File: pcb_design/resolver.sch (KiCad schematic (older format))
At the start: 0 parts

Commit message: Resolver routed using push pull buffer
Signed-off-by: Marcos Chaparro <mchaparro@paltatech.com>
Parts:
- added C73, C74, C75, C77, C81, C82, C83, C84, C85: 100nF, IPC7351-Nominal:CAPC1608X55, symbol C-0603
- added C76, C78: 4.7uF, IPC7351-Nominal:CAPC1608X55, symbol C-0603
- added C79, C80: 15p, IPC7351-Nominal:CAPC1608X55, symbol C
- added D21, D22, D23, D24: 1N4148W, smd-semi:SOD-123, symbol 1N4148W
- added E5: BEAD-220ohm@100khz, IPC7351-Nominal:INDC2012X130, symbol BEAD-0805
- added Q4, Q5: BC846BPDW1, smd-semi:SOT-363, symbol BC846BPDW1
- added R124, R125: 68k, IPC7351-Nominal:RESC1608X50, symbol R-0603
- added R126, R127, R128, R129, R130, R131, R132, R133: 10k, IPC7351-Nominal:RESC1608X50, symbol R-0603
- added R134, R137, R138, R141: 2.2k, IPC7351-Nominal:RESC1608X50, symbol R-0603
- added R135, R136, R139, R140: 3.3R, IPC7351-Nominal:RESC1608X50, symbol R-0603
- added R142, R143, R144, R145: 4.7R, IPC7351-Nominal:RESC2012X50, symbol R-0805
- added U15: AD2S1205, IPC7351-Nominal:QFP80P1200X1200X160-44, symbol AD2S1205
- added U18: SN74ALVC08PWR, IPC7351-Nominal:SOP65P640X110-14, symbol SN74ALVC08PWR
- added U19: OPA2376AID, IPC7351-Nominal:SOIC127P600X175-8, symbol OPA2376AID
- added X1: ABM3B - 8MHz, IPC7351-Nominal:OSCCC320X500X150, symbol XTAL-ABRACON-ABM3B
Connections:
- net labels added: +12, +3.3, +5, GND, ~RES_FAULT
- net labels removed: MOSI, ~FAULT
- wire segments 0 -> 137
- no-connect marks 0 -> 15
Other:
- note added: "5v tolerant?"
- note added: "Buffer"
- note added: "Resolver interface"
- note added: "doesn't support 12v!"
- note added: "needs voltage supervisor for ~RESET"

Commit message: Resolver routed. Added 12v regulator. The screw terminals were backwards(!). Started clearing up DRC markers.
Signed-off-by: Marcos Chaparro <mchaparro@paltatech.com>
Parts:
- removed D21, D22, D23, D24: 1N4148W, smd-semi:SOD-123, symbol 1N4148W
- removed Q4, Q5: BC846BPDW1, smd-semi:SOT-363, symbol BC846BPDW1
- removed R134, R137, R138, R141: 2.2k, IPC7351-Nominal:RESC1608X50, symbol R-0603
- removed R135, R136, R139, R140: 3.3R, IPC7351-Nominal:RESC1608X50, symbol R-0603
- removed R142, R143, R144, R145: 4.7R, IPC7351-Nominal:RESC2012X50, symbol R-0805
- removed U18: SN74ALVC08PWR, IPC7351-Nominal:SOP65P640X110-14, symbol SN74ALVC08PWR
- added C86, C87: 100nF, IPC7351-Nominal:CAPC1608X55, symbol C-0603
- added C88, C89: 22uF, IPC7351-Nominal:CAPC2012X70, symbol C-0805
- added E6: BEAD-220ohm@100khz, IPC7351-Nominal:INDC2012X130, symbol BEAD-0805
- added U18: AND3, smd-semi:SC-70-6, symbol AND3
- added U20: APX809, smd-semi:SOT-23, symbol APX809
- added U21: NCV78Mxx, smd-semi:TO-252, symbol NCV78Mxx
- C83, C84: value 100nF -> 120pF
- R127, R129: value 10k -> 22k
- R132, R133: value 10k -> 15.4k
- U19: value OPA2376AID -> AD8397; BOM IC TI OPA2376AID -> IC AD8397ARZ; mfg# OPA2376AIDR -> AD8397ARZ
- U19: value OPA2376AID -> AD8397; BOM IC TI OPA2376AID -> IC AD8397ARZ; mfg# (none) -> AD8397ARZ
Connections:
- net labels added: +24, EXC_SOURCE+, EXC_SOURCE-
- net labels removed: ~RD
- wire segments 137 -> 110
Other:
- note added: "RESET line requires\na voltage monitor"
- note added: "This is an alternative buffer suggested here:\nhttp://www.analog.com/en/analog-dialogue/articles/precision-rtdc-measures-angular-position-and-velocity.html\nIts more expensive, but much simpler and smaller"
- note removed: "5v tolerant?"
- note removed: "doesn't support 12v!"
- note removed: "needs voltage supervisor for ~RESET"
- moved on the sheet: C73, C74, C76, C77, C78, C79, C80, C81, C82, C83, C84, C85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

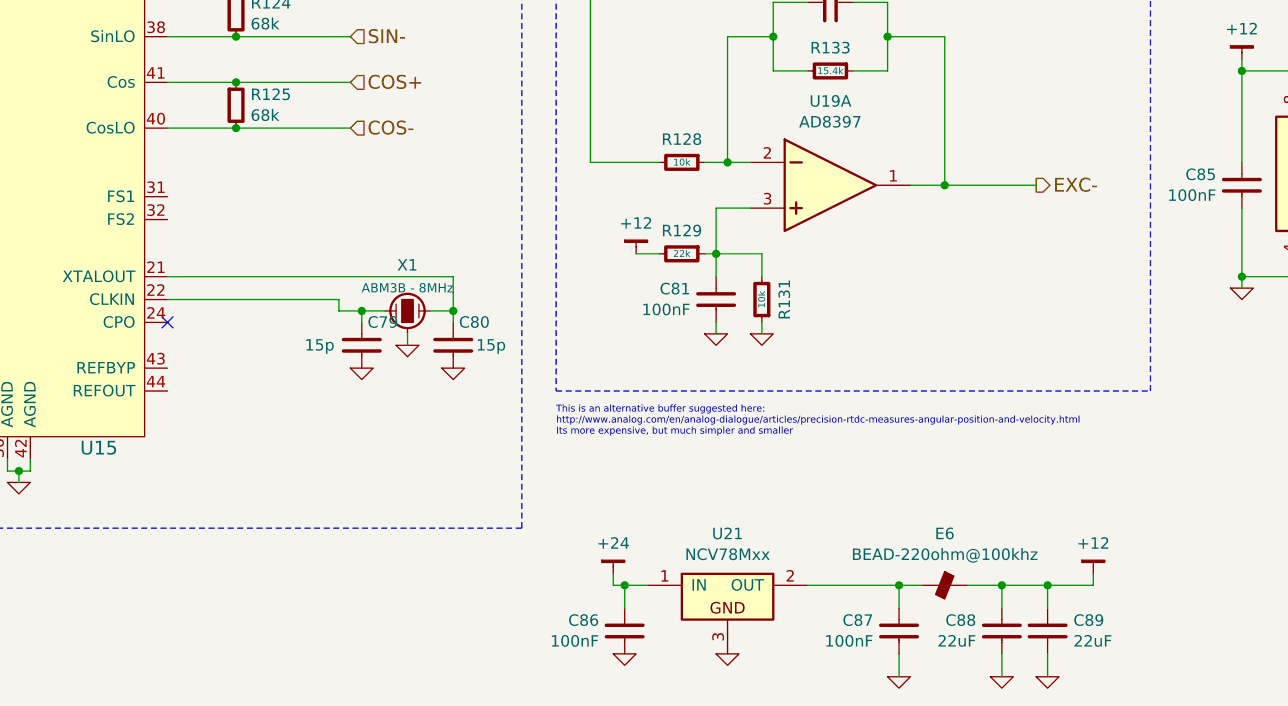
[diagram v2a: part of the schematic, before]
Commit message: Routing complete. Added 3D models. No DRC errors, a few ERC warnings
Signed-off-by: Marcos Chaparro <mchaparro@paltatech.com>
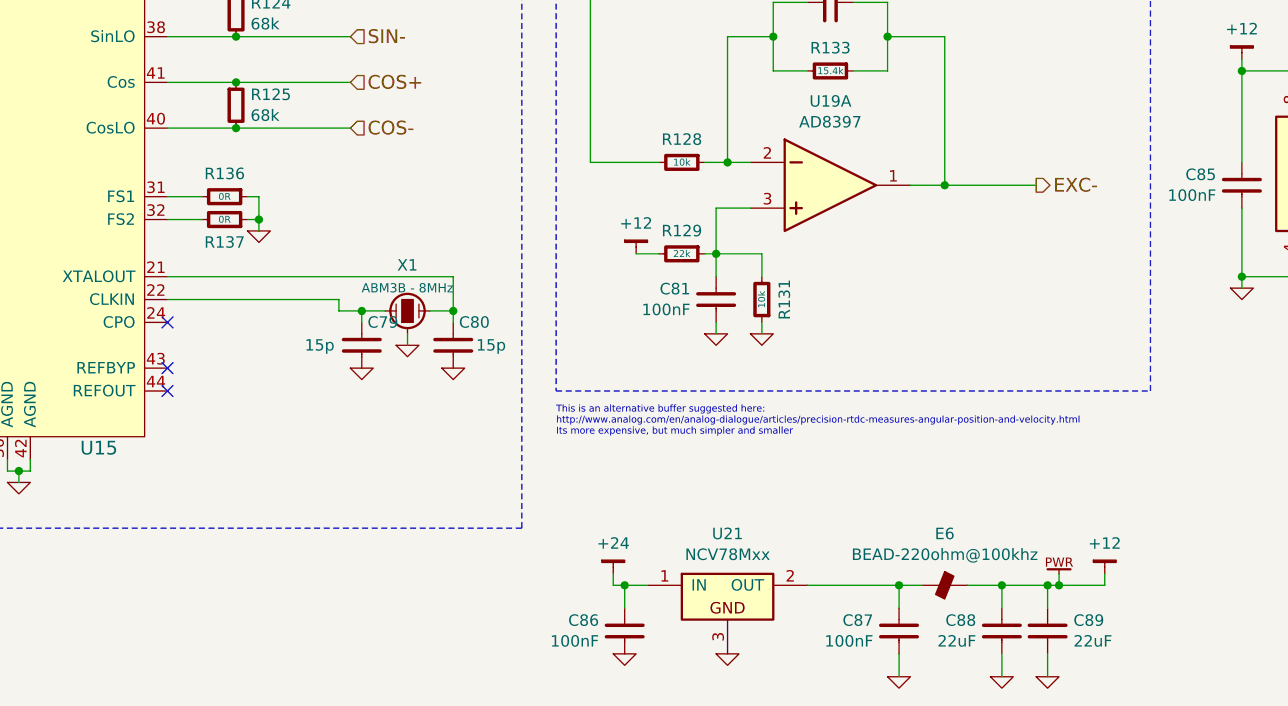
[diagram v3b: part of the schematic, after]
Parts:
- added R136, R137: 0R, IPC7351-Nominal:RESC1608X50, symbol R-0603
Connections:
- net GND: now also R136.1, R137.1
- net at U15.31 (FS1): now also R136.2
- net at U15.32 (FS2): now also R137.2
- no-connect marks 15 -> 17

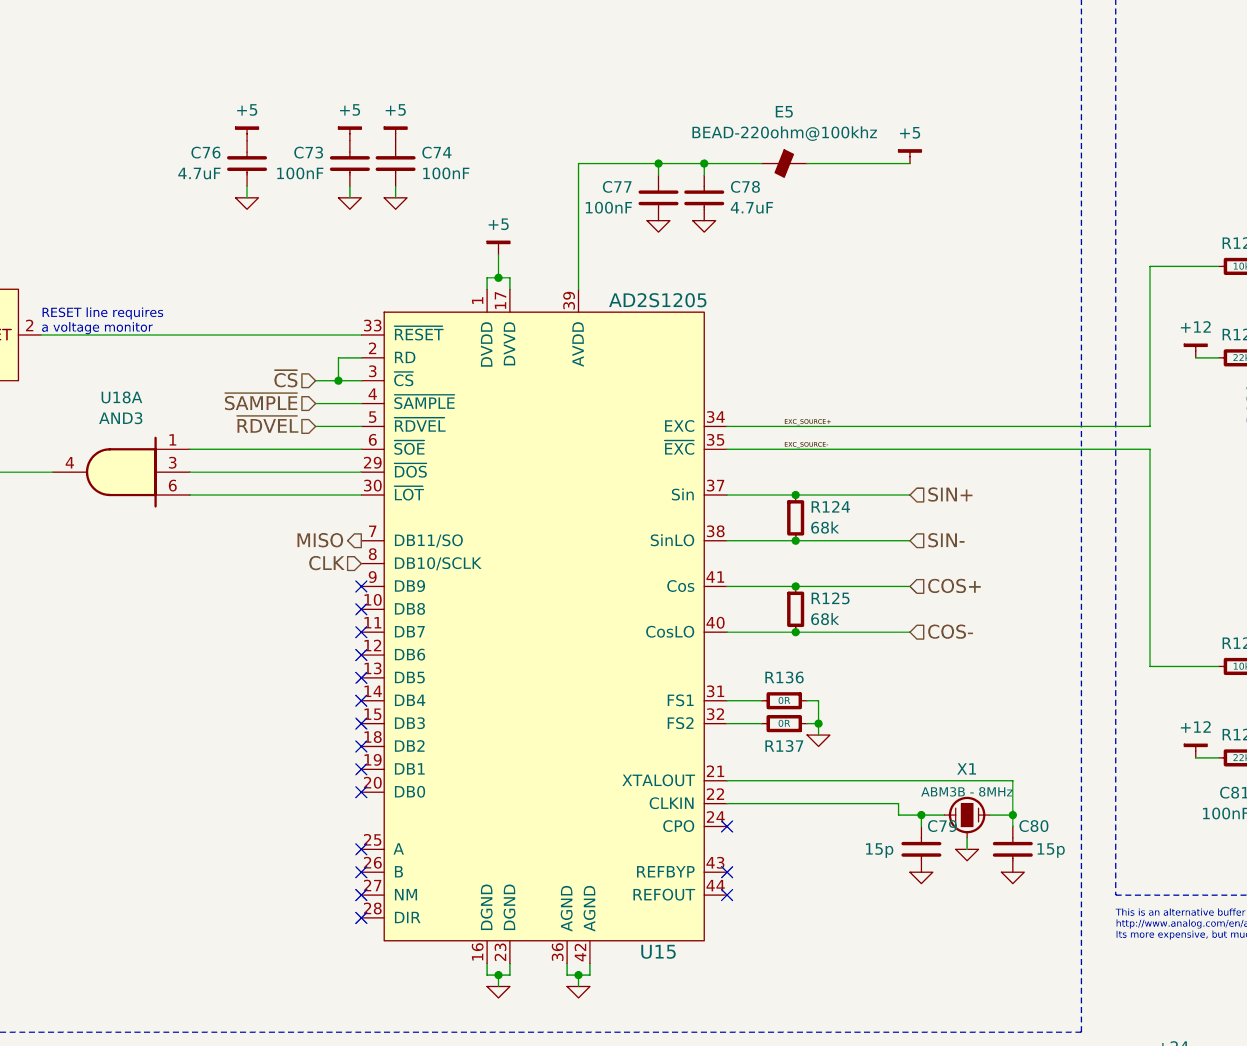
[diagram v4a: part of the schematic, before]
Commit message: Completed some part numbers
Signed-off-by: Marcos Chaparro <mchaparro@paltatech.com>
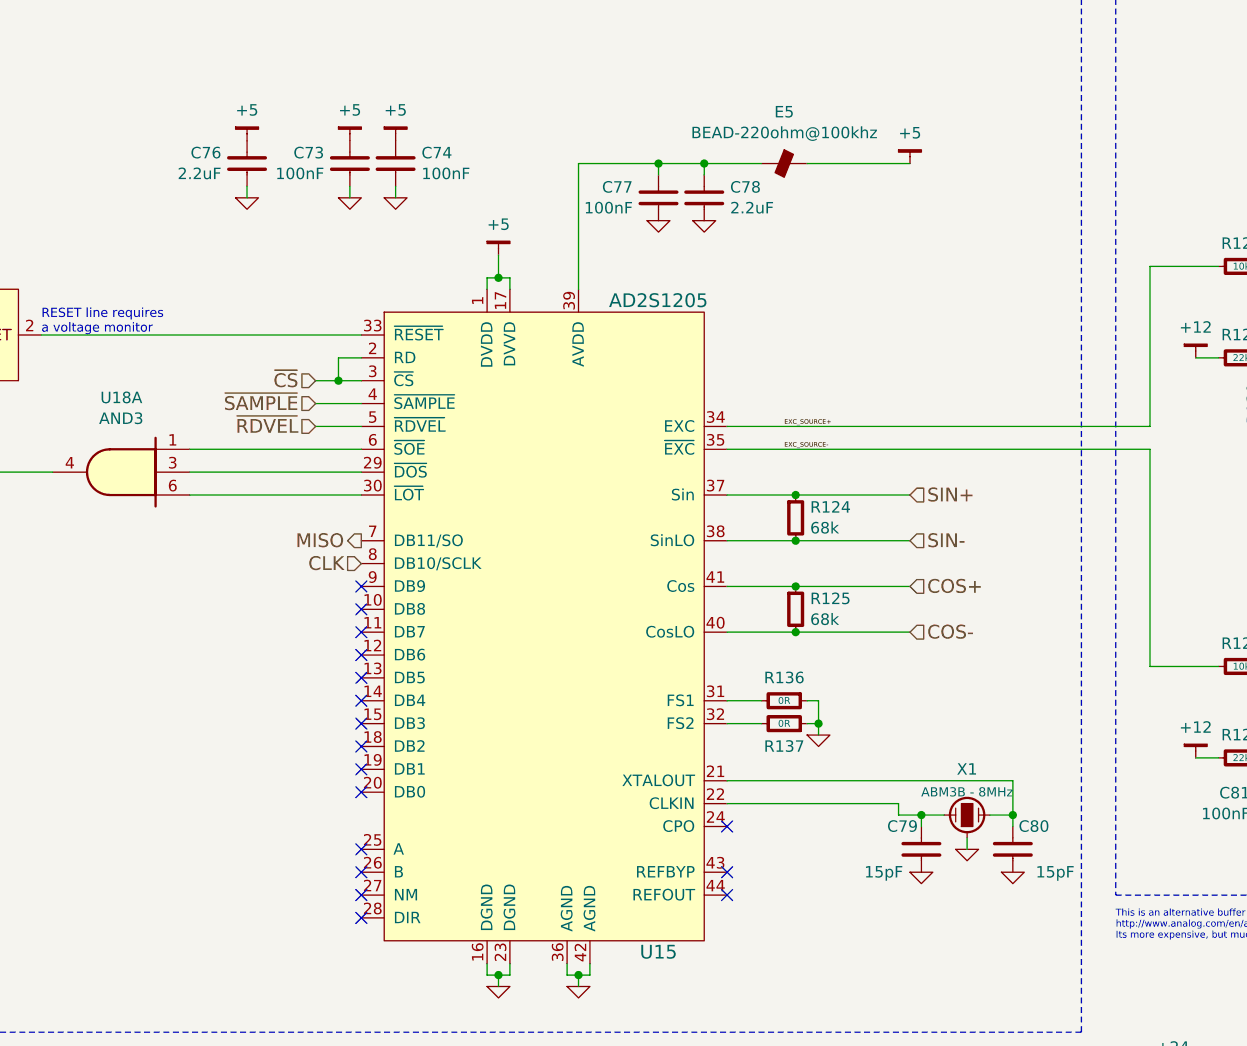
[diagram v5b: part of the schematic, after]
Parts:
- C73, C74, C75, C77, C81, C82, C85, C86, C87: MFR (none) -> Murata Electronics North America; MPN (none) -> GRM188R71E104KA01D; SPN (none) -> 490-1524-1-ND; SPR (none) -> Digikey
- C76, C78: value 4.7uF -> 2.2uF; MFR (none) -> Murata Electronics North America; MPN (none) -> GRM188R71A225KE15D; SPN (none) -> 490-4520-1-ND; SPR (none) -> Digikey
- C79, C80: value 15p -> 15pF; MFR (none) -> Murata Electronics North America; MPN (none) -> GCM1885C1H150JA16D; SPN (none) -> 490-4957-1-ND; SPR (none) -> Digikey
- C83, C84: MFR (none) -> KEMET; MPN (none) -> C0603C121F5GACTU; SPN (none) -> 399-7850-1-ND; SPR (none) -> Digikey
- C88, C89: MFR (none) -> TDK Corporation; MPN (none) -> C2012X5R1V226M125AC; SPN (none) -> 445-14428-1-ND; SPR (none) -> Digikey

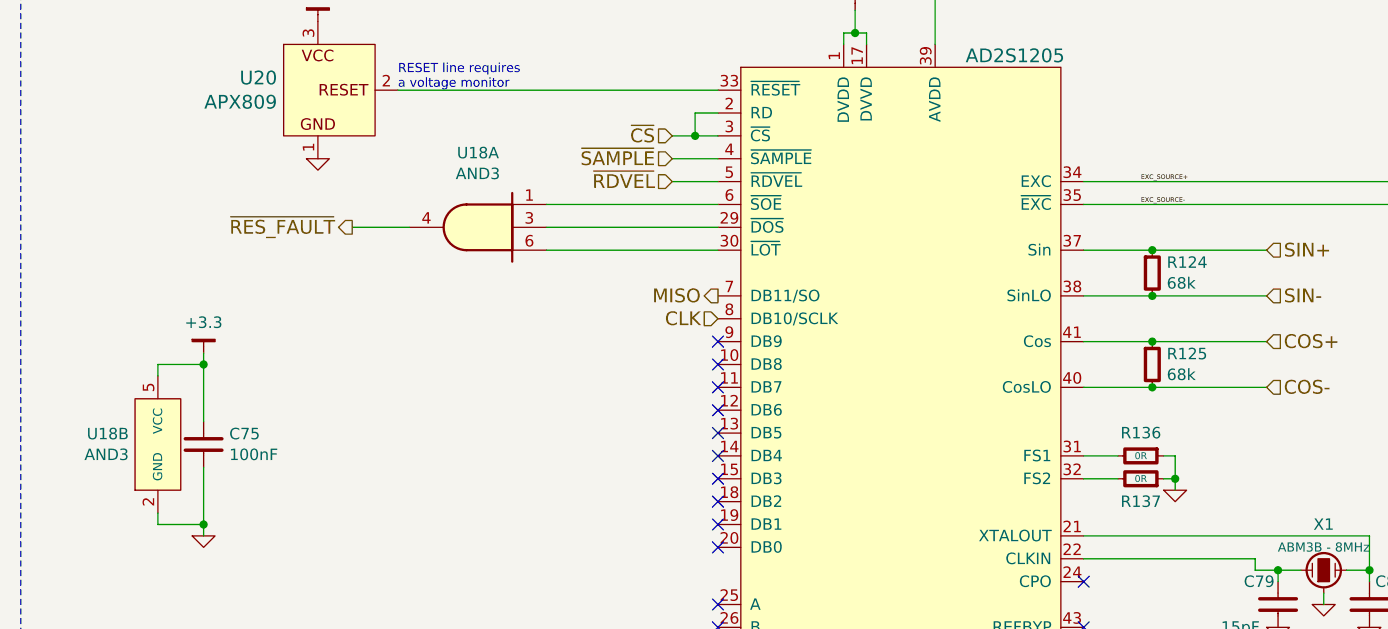
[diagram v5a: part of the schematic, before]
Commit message: Completed part number, manufacturer, etc fields. Simulated analog conditioning
Signed-off-by: Marcos Chaparro <mchaparro@paltatech.com>
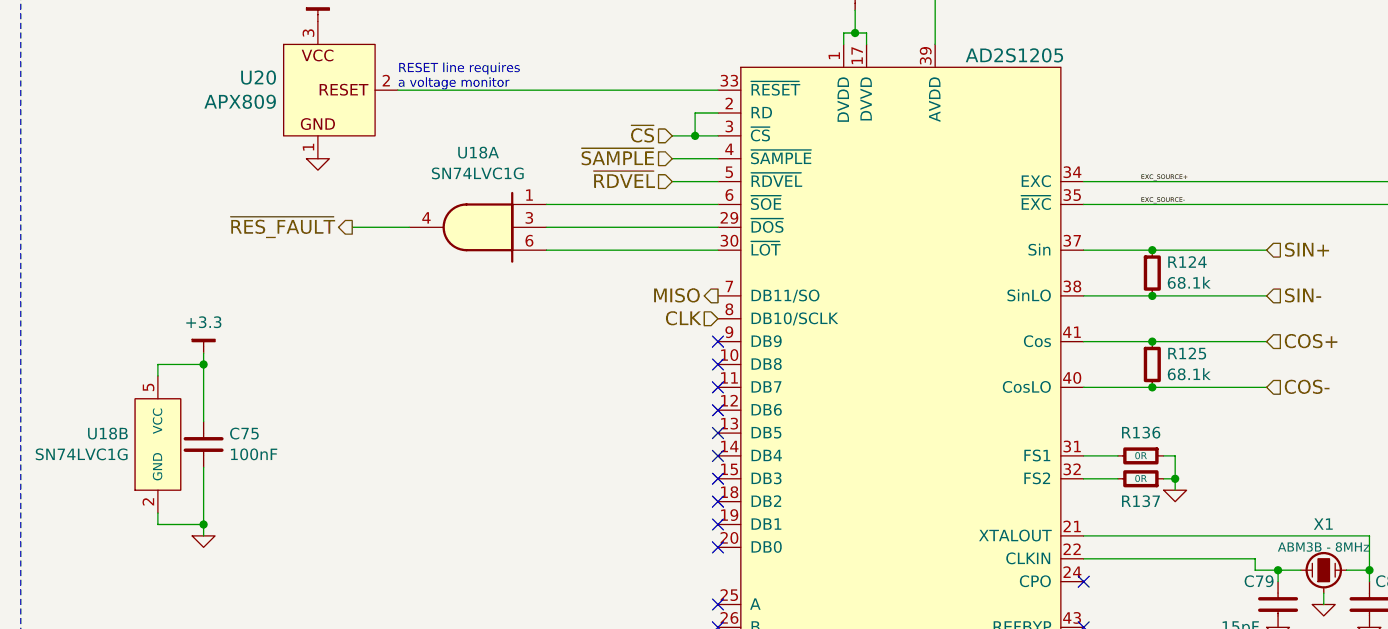
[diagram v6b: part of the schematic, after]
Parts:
- E5, E6: MFR (none) -> Murata Electronics North America; MPN (none) -> BLM21PG221SN1D; SPN (none) -> 490-1054-1-ND; SPR (none) -> Digikey
- R124, R125: value 68k -> 68.1k; MFR (none) -> Yageo; MPN (none) -> RC0603FR-0768K1L; SPN (none) -> 311-68.1KHRCT-ND; SPR (none) -> Digikey
- R126, R128, R130, R131: MFR (none) -> Yageo; MPN (none) -> RC0603FR-0710KL; SPN (none) -> 311-10.0KHRCT-ND; SPR (none) -> Digikey
- R127, R129: MFR (none) -> Yageo; MPN (none) -> RC0603FR-0722KL; SPN (none) -> 311-22.0KHRCT-ND; SPR (none) -> Digikey
- R132, R133: MFR (none) -> Yageo; MPN (none) -> RC0603FR-0715K4L; SPN (none) -> 311-15.4KHRCT-ND; SPR (none) -> Digikey
- R136, R137: MFR (none) -> Yageo; MPN (none) -> RC0603JR-070RL; SPN (none) -> 311-0.0GRCT-ND; SPR (none) -> Digikey
- U15: MFR (none) -> Analog Devices Inc.; MPN (none) -> AD2S1205YSTZ; SPN (none) -> AD2S1205YSTZ-ND; SPR (none) -> Digikey
- U18: value AND3 -> SN74LVC1G; MFR (none) -> Texas Instruments; MPN (none) -> SN74LVC1G11IDCKRQ1; SPN (none) -> 296-36722-1-ND; SPR (none) -> Digikey
- U19: MFR (none) -> Analog Devices Inc.; MPN (none) -> AD8397ARZ; SPN (none) -> AD8397ARZ-ND; SPR (none) -> Digikey
- U20: MFR (none) -> Diodes Incorporated; MPN (none) -> APX809-46SRG-7; SPN (none) -> APX809-46SRGDICT-ND; SPR (none) -> Digikey
- U21: MFR (none) -> ON Semiconductor; MPN (none) -> NCV78M12BDTRKG; SPN (none) -> NCV78M12BDTRKGOSCT-ND; SPR (none) -> Digikey
- X1: MFR (none) -> Abracon LLC; MPN (none) -> ABM3B-8.000MHZ-10-1UT; SPN (none) -> 535-9721-1-ND; SPR (none) -> Digikey
